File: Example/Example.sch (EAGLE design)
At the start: 11 parts, among them IC1 LM555D, J1 UX60-MB-5S8, Q2 BSS806N, SW1 MFS101D-6-Z

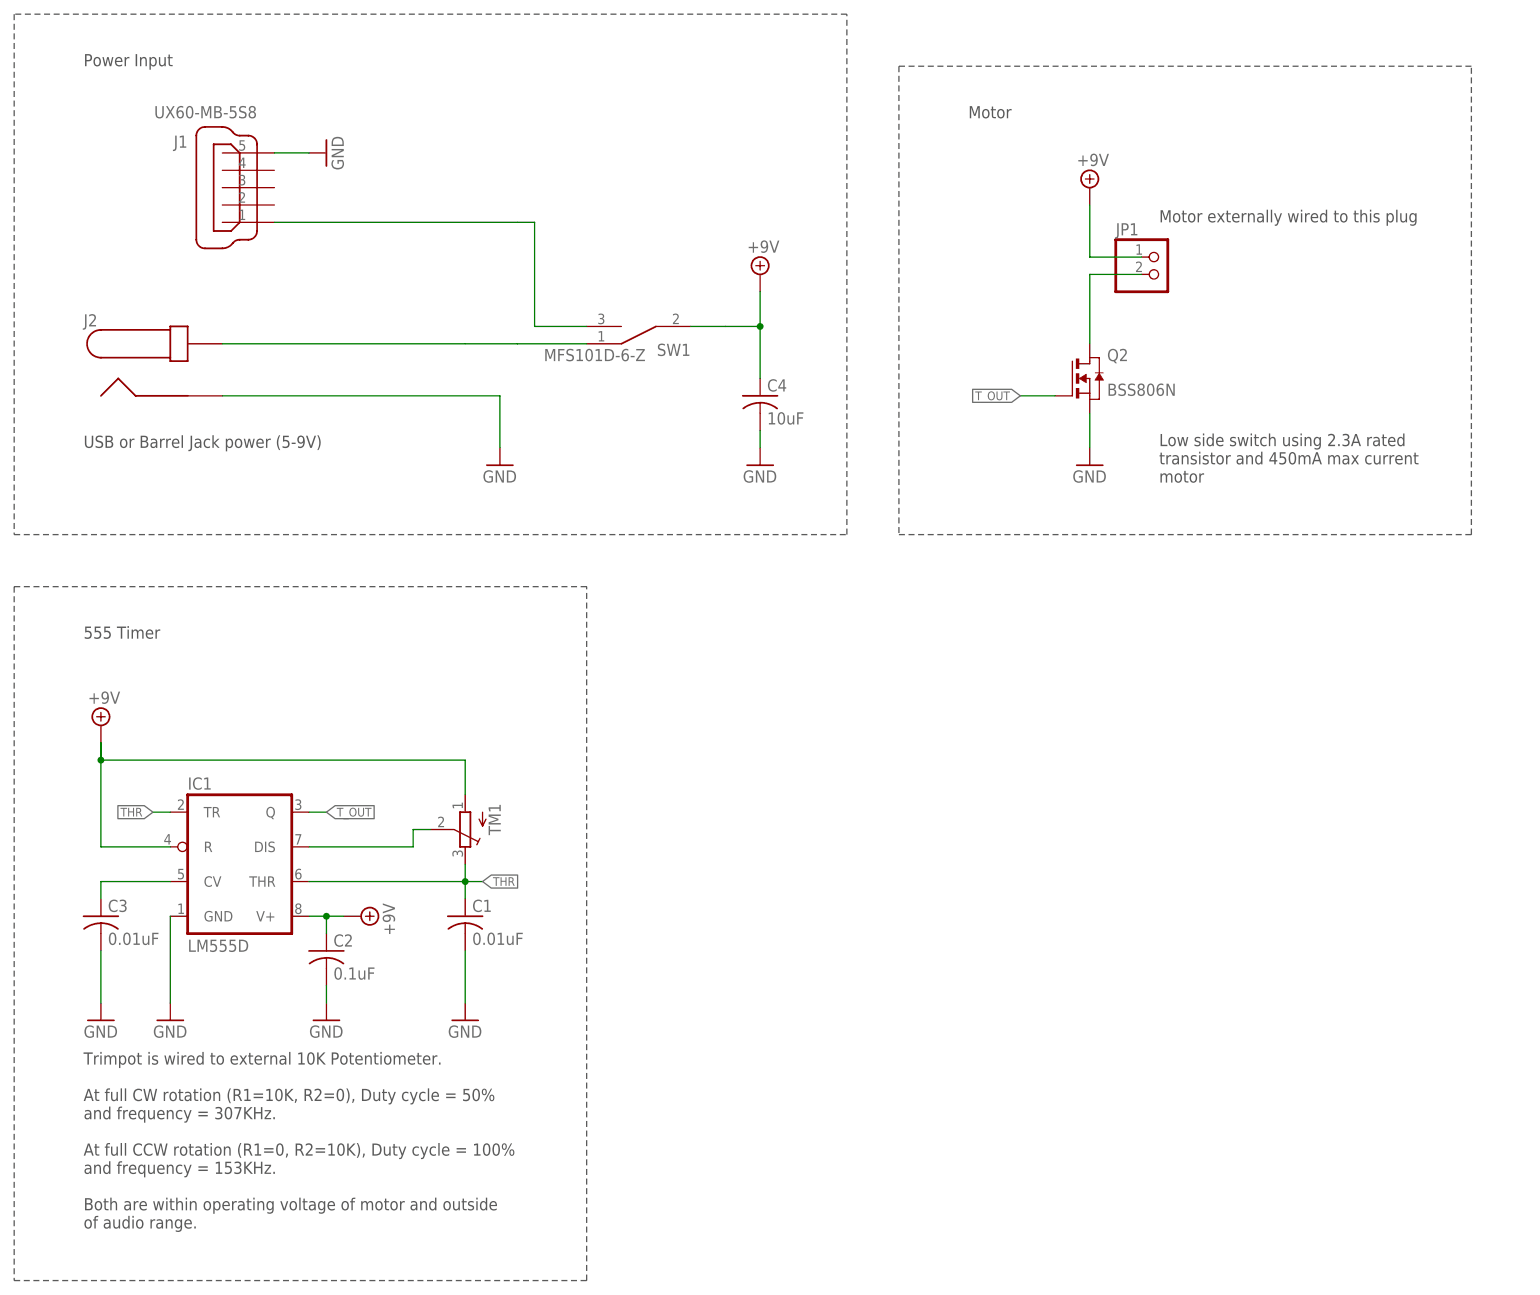
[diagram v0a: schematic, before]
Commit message: Made footprints for motors, battery case, and guiding spring
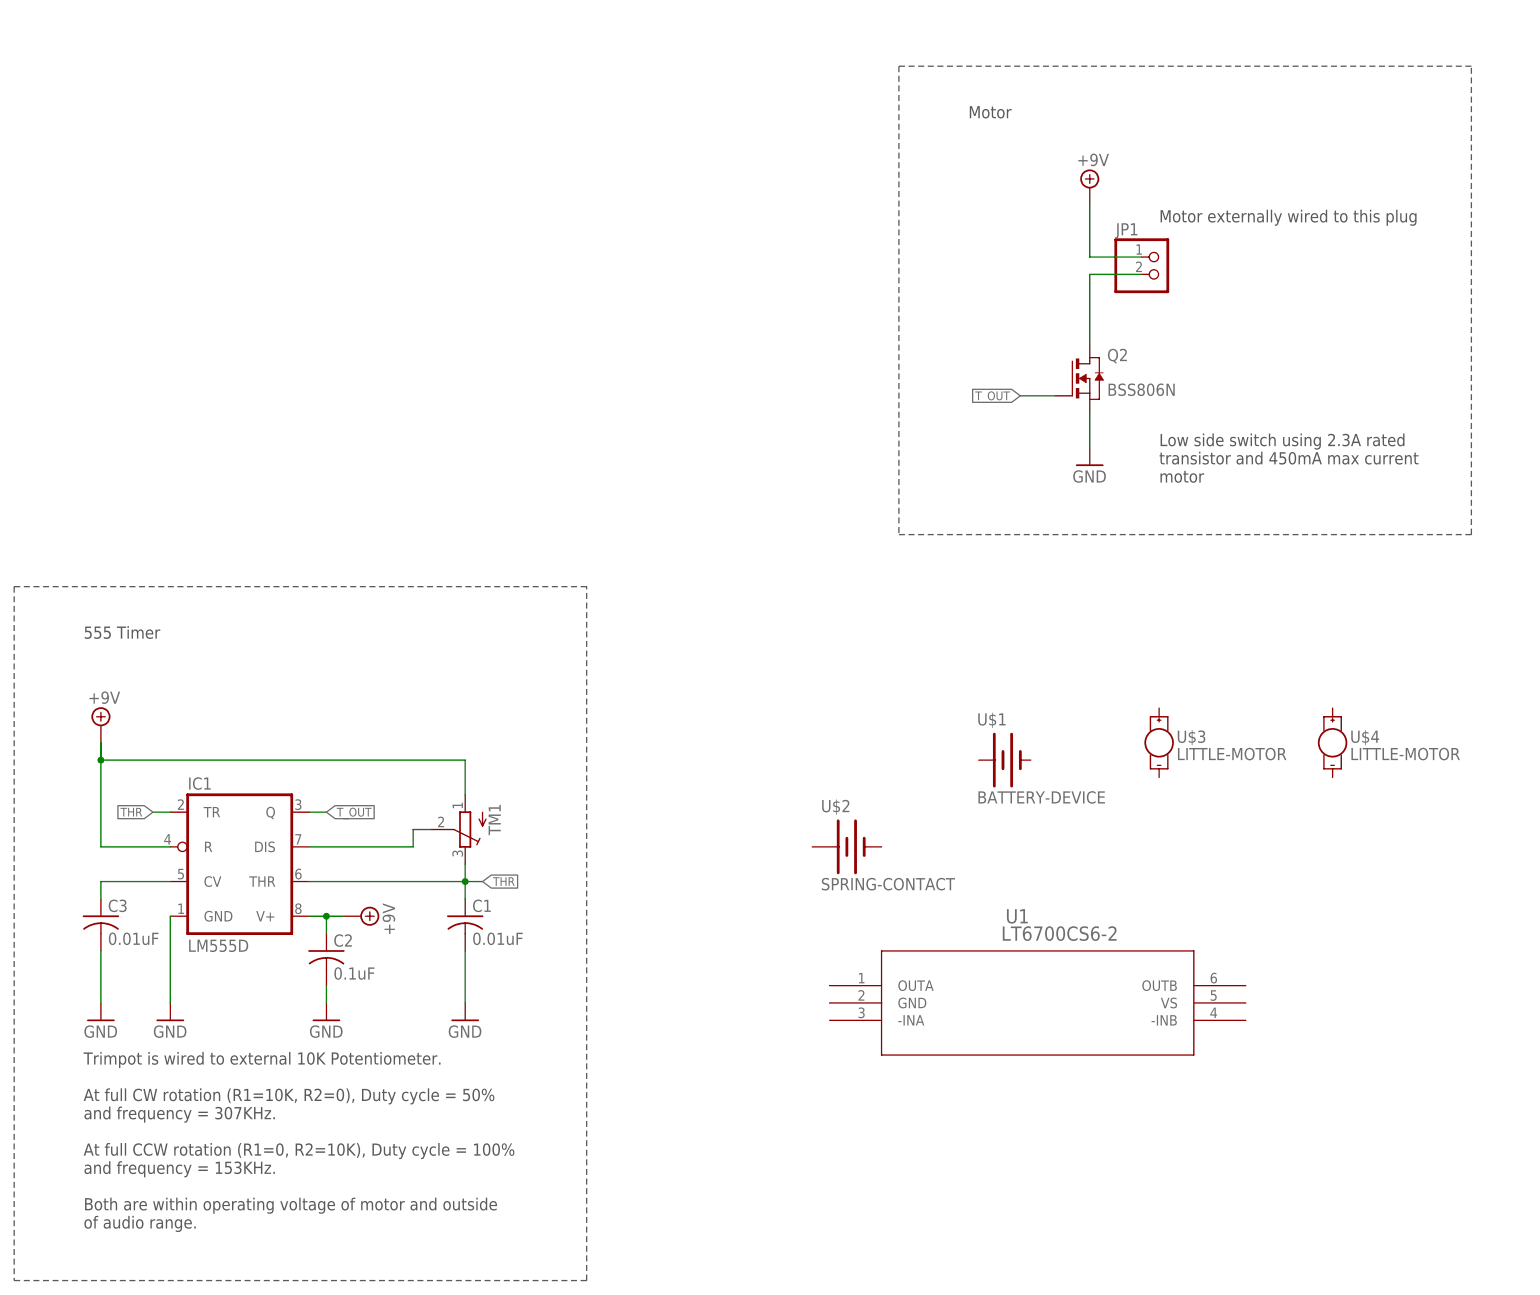
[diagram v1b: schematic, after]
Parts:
- removed C4: 10uF, rcl:C-USC0603
- removed J1: UX60-MB-5S8, RoboJackets-Connectors:UX60-MB-5S8
- removed J2: (no value), RoboJackets-Connectors:PJ-037A
- removed SW1: MFS101D-6-Z, Example:MFS101D-6-Z
- added U$1: BATTERY-DEVICE, battery-stringshooter-holder-18650:BATTERY-DEVICE
- added U$2: SPRING-CONTACT, battery-contact-AA:SPRING-CONTACT
- added U$3, U$4: LITTLE-MOTOR, motor-stringshooter:LITTLE-MOTOR
- added U1: LT6700CS6-2, LT6700CS6-2:LT6700CS6-2
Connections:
- removed net N$4: J1.1, SW1.B
- removed net N$6: J2.1, SW1.A
- net +9V: no longer C4.1, SW1.COMMON
- net GND: no longer C4.2, J1.5, J2.2
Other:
- note removed: "Power Input"
- note removed: "USB or Barrel Jack power (5-9V)"
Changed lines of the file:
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@@
 <?xml version="1.0" encoding="utf-8"?>
 <!DOCTYPE eagle SYSTEM "eagle.dtd">
-<eagle version="9.5.2">
+<eagle version="9.6.2">
 <drawing>
 <settings>
@@
 <part name="Q2" library="RoboJackets-Discrete" deviceset="BSS806N" device="" override_package3d_urn="urn:adsk.eagle:package:25000917/2" override_package_urn="urn:adsk.eagle:footprint:25000918/1"/>
 <part name="SUPPLY6" library="RoboJackets-Supplies" deviceset="GND" device=""/>
-<part name="J2" library="RoboJackets-Connectors" deviceset="PJ-037A*" device="" override_package3d_urn="urn:adsk.eagle:package:25000921/2" override_package_urn="urn:adsk.eagle:footprint:25000922/1"/>
 <part name="JP1" library="RoboJackets-Connectors" deviceset="PINHD-1X2" device="" package3d_urn="urn:adsk.eagle:package:22435/2"/>
 <part name="SUPPLY7" library="RoboJackets-Supplies" deviceset="+9V" device=""/>
-<part name="SUPPLY8" library="RoboJackets-Supplies" deviceset="GND" device=""/>
-<part name="SUPPLY9" library="RoboJackets-Supplies" deviceset="+9V" device=""/>
 <part name="SUPPLY10" library="RoboJackets-Supplies" deviceset="GND" device=""/>
-<part name="J1" library="RoboJackets-Connectors" deviceset="UX60*-MB-5S?" device="8" override_package3d_urn="urn:adsk.eagle:package:25000186/2" override_package_urn="urn:adsk.eagle:footprint:25000187/1"/>
-<part name="SUPPLY11" library="RoboJackets-Supplies" deviceset="GND" device=""/>
-<part name="C4" library="rcl" library_urn="urn:adsk.eagle:library:334" deviceset="C-US" device="C0603" package3d_urn="urn:adsk.eagle:package:23616/2" value="10uF"/>
-<part name="SUPPLY12" library="RoboJackets-Supplies" deviceset="GND" device=""/>
-<part name="SW1" library="Example" deviceset="MFS101D-6-Z" device="" override_package3d_urn="urn:adsk.eagle:package:25000897/2" override_package_urn="urn:adsk.eagle:footprint:25000899/1"/>
+<part name="U1" library="LT6700CS6-2" deviceset="LT6700CS6-2" device=""/>
+<part name="U$1" library="battery-stringshooter-holder-18650" deviceset="BATTERY-DEVICE" device=""/>
+<part name="U$3" library="motor-stringshooter" deviceset="LITTLE-MOTOR" device=""/>
+<part name="U$4" library="motor-stringshooter" deviceset="LITTLE-MOTOR" device=""/>
+<part name="U$2" library="battery-contact-AA" deviceset="SPRING-CONTACT" device=""/>
 </parts>
 <sheets>
@@
 transistor and 450mA max current
 motor</text>
-<text x="25.4" y="139.7" size="1.778" layer="97">USB or Barrel Jack power (5-9V)</text>
-<wire x1="15.24" y1="127" x2="137.16" y2="127" width="0.1524" layer="97" style="shortdash"/>
-<wire x1="137.16" y1="127" x2="137.16" y2="203.2" width="0.1524" layer="97" style="shortdash"/>
-<wire x1="137.16" y1="203.2" x2="15.24" y2="203.2" width="0.1524" layer="97" style="shortdash"/>
-<wire x1="15.24" y1="203.2" x2="15.24" y2="127" width="0.1524" layer="97" style="shortdash"/>
-<text x="25.4" y="195.58" size="1.778" layer="97">Power Input</text>
 <wire x1="15.24" y1="119.38" x2="15.24" y2="17.78" width="0.1524" layer="97" style="shortdash"/>
 <wire x1="15.24" y1="17.78" x2="99.06" y2="17.78" width="0.1524" layer="97" style="shortdash"/>
@@
 <attribute name="VALUE" x="170.18" y="134.62" size="1.778" layer="96"/>
 </instance>
-<instance part="J2" gate="G$1" x="35.56" y="149.86" smashed="yes">
-<attribute name="NAME" x="25.4" y="157.48" size="1.778" layer="95"/>
-<attribute name="VALUE" x="25.4" y="144.78" size="1.778" layer="96"/>
-</instance>
 <instance part="JP1" gate="G$1" x="182.88" y="165.1" smashed="yes">
 <attribute name="NAME" x="176.53" y="170.815" size="1.778" layer="95"/>
@@
 <attribute name="VALUE" x="170.815" y="180.975" size="1.778" layer="96"/>
 </instance>
-<instance part="SUPPLY8" gate="G$1" x="86.36" y="137.16" smashed="yes">
-<attribute name="VALUE" x="83.82" y="134.62" size="1.778" layer="96"/>
-</instance>
-<instance part="SUPPLY9" gate="+9V" x="124.46" y="165.1" smashed="yes">
-<attribute name="VALUE" x="122.555" y="168.275" size="1.778" layer="96"/>
-</instance>
 <instance part="SUPPLY10" gate="G$1" x="27.94" y="55.88" smashed="yes">
 <attribute name="VALUE" x="25.4" y="53.34" size="1.778" layer="96"/>
 </instance>
-<instance part="J1" gate="G$1" x="48.26" y="177.8" smashed="yes" rot="R180">
-<attribute name="NAME" x="40.64" y="185.42" size="1.778" layer="95" rot="R180"/>
-<attribute name="VALUE" x="50.8" y="187.96" size="1.778" layer="96" rot="R180" align="top-left"/>
-</instance>
-<instance part="SUPPLY11" gate="G$1" x="60.96" y="182.88" smashed="yes" rot="R90">
-<attribute name="VALUE" x="63.5" y="180.34" size="1.778" layer="96" rot="R90"/>
-</instance>
-<instance part="C4" gate="G$1" x="124.46" y="147.32" smashed="yes">
-<attribute name="NAME" x="125.476" y="147.955" size="1.778" layer="95"/>
-<attribute name="VALUE" x="125.476" y="143.129" size="1.778" layer="96"/>
-</instance>
-<instance part="SUPPLY12" gate="G$1" x="124.46" y="137.16" smashed="yes">
-<attribute name="VALUE" x="121.92" y="134.62" size="1.778" layer="96"/>
-</instance>
-<instance part="SW1" gate="G$1" x="106.68" y="157.48" smashed="yes" rot="R180">
-<attribute name="NAME" x="114.3" y="154.94" size="1.778" layer="95" rot="R180"/>
-<attribute name="VALUE" x="107.696" y="154.178" size="1.778" layer="96" rot="R180"/>
+<instance part="U1" gate="A" x="134.62" y="60.96" smashed="yes">
+<attribute name="NAME" x="160.3756" y="70.0786" size="2.0828" layer="95" ratio="6" rot="SR0"/>
+<attribute name="VALUE" x="159.7406" y="67.5386" size="2.0828" layer="96" ratio="6" rot="SR0"/>
+</instance>
+<instance part="U$1" gate="G$1" x="160.02" y="93.98" smashed="yes">
+<attribute name="NAME" x="156.21" y="99.06" size="1.778" layer="95"/>
+<attribute name="VALUE" x="156.21" y="87.63" size="1.778" layer="96"/>
+</instance>
+<instance part="U$3" gate="G$1" x="182.88" y="96.52" smashed="yes">
+<attribute name="NAME" x="185.42" y="96.52" size="1.778" layer="95" font="vector"/>
+<attribute name="VALUE" x="185.42" y="93.98" size="1.778" layer="96" font="vector"/>
+</instance>
+<instance part="U$4" gate="G$1" x="208.28" y="96.52" smashed="yes">
+<attribute name="NAME" x="210.82" y="96.52" size="1.778" layer="95" font="vector"/>
+<attribute name="VALUE" x="210.82" y="93.98" size="1.778" layer="96" font="vector"/>
+</instance>
+<instance part="U$2" gate="G$1" x="137.16" y="81.28" smashed="yes">
+<attribute name="NAME" x="133.35" y="86.36" size="1.778" layer="95"/>
+<attribute name="VALUE" x="133.35" y="74.93" size="1.778" layer="96"/>
 </instance>
 </instances>
@@
 </segment>
 <segment>
-<pinref part="J2" gate="G$1" pin="2"/>
-<wire x1="45.72" y1="147.32" x2="86.36" y2="147.32" width="0.1524" layer="91"/>
-<pinref part="SUPPLY8" gate="G$1" pin="GND"/>
-<wire x1="86.36" y1="147.32" x2="86.36" y2="139.7" width="0.1524" layer="91"/>
-</segment>
-<segment>
 <pinref part="SUPPLY10" gate="G$1" pin="GND"/>
 <pinref part="C3" gate="G$1" pin="2"/>
 <wire x1="27.94" y1="58.42" x2="27.94" y2="66.04" width="0.1524" layer="91"/>
-</segment>
-<segment>
-<pinref part="J1" gate="G$1" pin="5"/>
-<wire x1="53.34" y1="182.88" x2="58.42" y2="182.88" width="0.1524" layer="91"/>
-<pinref part="SUPPLY11" gate="G$1" pin="GND"/>
-</segment>
-<segment>
-<pinref part="SUPPLY12" gate="G$1" pin="GND"/>
-<pinref part="C4" gate="G$1" pin="2"/>
-<wire x1="124.46" y1="139.7" x2="124.46" y2="142.24" width="0.1524" layer="91"/>
 </segment>
 </net>
@@
 <pinref part="SUPPLY7" gate="+9V" pin="+9V"/>
 </segment>
-<segment>
-<pinref part="SUPPLY9" gate="+9V" pin="+9V"/>
-<wire x1="124.46" y1="157.48" x2="124.46" y2="162.56" width="0.1524" layer="91"/>
-<wire x1="114.3" y1="157.48" x2="119.38" y2="157.48" width="0.1524" layer="91"/>
-<wire x1="119.38" y1="157.48" x2="124.46" y2="157.48" width="0.1524" layer="91"/>
-<pinref part="C4" gate="G$1" pin="1"/>
-<wire x1="124.46" y1="149.86" x2="124.46" y2="157.48" width="0.1524" layer="91"/>
-<junction x="124.46" y="157.48"/>
-<pinref part="SW1" gate="G$1" pin="COMMON"/>
-</segment>
 </net>
 <net name="THR" class="0">
@@
 </segment>
 </net>
-<net name="N$4" class="0">
-<segment>
-<pinref part="J1" gate="G$1" pin="1"/>
-<wire x1="53.34" y1="172.72" x2="88.9" y2="172.72" width="0.1524" layer="91"/>
-<wire x1="88.9" y1="172.72" x2="91.44" y2="172.72" width="0.1524" layer="91"/>
-<wire x1="91.44" y1="172.72" x2="91.44" y2="157.48" width="0.1524" layer="91"/>
-<wire x1="91.44" y1="157.48" x2="93.98" y2="157.48" width="0.1524" layer="91"/>
-<pinref part="SW1" gate="G$1" pin="B"/>
-<wire x1="93.98" y1="157.48" x2="99.06" y2="157.48" width="0.1524" layer="91"/>
-</segment>
-</net>
-<net name="N$6" class="0">
-<segment>
-<pinref part="J2" gate="G$1" pin="1"/>
-<wire x1="45.72" y1="154.94" x2="81.28" y2="154.94" width="0.1524" layer="91"/>
-<wire x1="81.28" y1="154.94" x2="88.9" y2="154.94" width="0.1524" layer="91"/>
-<pinref part="SW1" gate="G$1" pin="A"/>
-<wire x1="99.06" y1="154.94" x2="88.9" y2="154.94" width="0.1524" layer="91"/>
-</segment>
-</net>
